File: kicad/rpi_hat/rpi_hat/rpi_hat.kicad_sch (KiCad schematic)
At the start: 12 parts, among them J1 FrontButtons, J2 PowerButton, J3 PowerWakeup, J4 DisplaySPI, J5 BatteryLevel, J6 GPIO, Q1 AO3401A, Q2 PN2222A

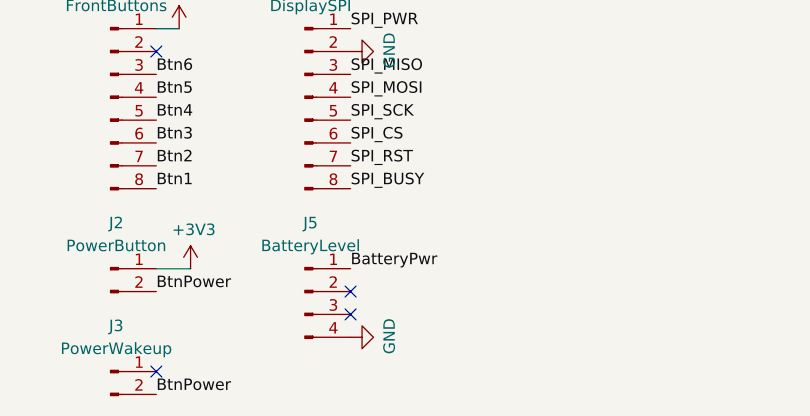
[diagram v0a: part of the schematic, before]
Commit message: add script to read voltage from adc and fix hat
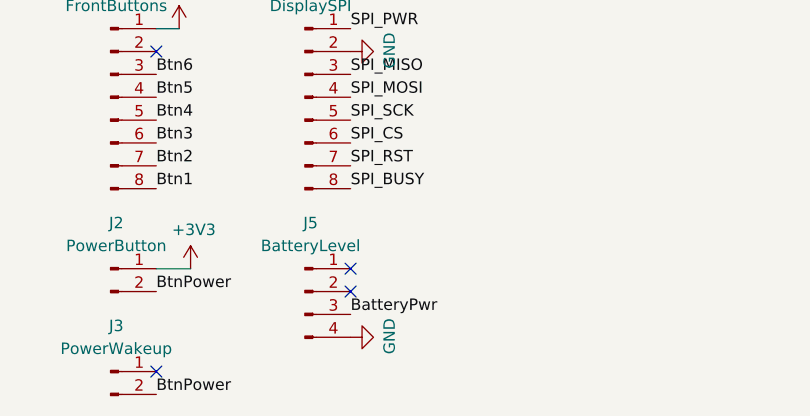
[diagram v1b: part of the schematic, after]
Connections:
- net BatteryPwr: now also J5.3 (Pin_3); no longer J5.1 (Pin_1)
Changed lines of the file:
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@@
+	)
+	(no_connect
+		(at 67.31 134.62)
 	)
 	(no_connect
@@
 	(no_connect
 		(at 109.22 88.9)
-	)
-	(no_connect
-		(at 67.31 139.7)
 	)
 	(no_connect
@@
 		)
 	)
-	(label "BatteryPwr"
-		(at 67.31 134.62 0)
-		(effects
-			(font
-				(size 1.27 1.27)
-			)
-			(justify left bottom)
-		)
-	)
 	(label "GPIO14{slash}TXD0"
 		(at 109.22 50.8 180)
@@
 		(effects
 			(font
+				(size 1.27 1.27)
+			)
+			(justify left bottom)
+		)
+	)
+	(label "BatteryPwr"
+		(at 67.31 139.7 0)
+		(effects
+			(font

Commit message: wip
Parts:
- added R5: 10k, Resistor_THT:R_Axial_DIN0207_L6.3mm_D2.5mm_P10.16mm_Horizontal, symbol Device:R
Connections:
- net +3V3: no longer J2.1 (Pin_1)
- net BtnPower: now also J2.1 (Pin_1), R5.2; no longer J2.2 (Pin_2), J3.2 (Pin_2)
- net GND: now also J2.2 (Pin_2)
- net at J3.1 (Pin_1): now also R5.1

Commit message: finish battery support
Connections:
- net GND: no longer J5.4 (Pin_4), J6.33 (Pin_33), R2.1
- new net BatterNNP16: J5.4 (Pin_4), J6.33 (Pin_33), R2.1
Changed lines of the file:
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@@
+		)
+	)
+	(label "BatteryGND"
+		(at 67.31 142.24 0)
+		(effects
+			(font
+				(size 1.27 1.27)
+			)
+			(justify left bottom)
 		)
 	)
@@
 			)
 			(justify left bottom)
+		)
+	)
+	(label "BatteryGND"
+		(at 187.96 139.7 270)
+		(effects
+			(font
+				(size 1.27 1.27)
+			)
+			(justify right bottom)
 		)
 	)
@@
 	)
 	(symbol
-		(lib_id "power:GND")
-		(at 187.96 139.7 0)
-		(unit 1)
-		(body_style 1)
-		(exclude_from_sim no)
-		(in_bom yes)
-		(on_board yes)
-		(in_pos_files yes)
-		(dnp no)
-		(property "Reference" "#PWR08"
-			(at 187.96 146.05 0)
-			(hide yes)
-			(show_name no)
-			(do_not_autoplace no)
-			(effects
-				(font
-					(size 1.27 1.27)
-				)
-			)
-		)
-		(property "Value" "GND"
-			(at 188.0743 144.0244 0)
-			(show_name no)
-			(do_not_autoplace no)
-			(effects
-				(font
-					(size 1.27 1.27)
-				)
-			)
-		)
-		(property "Footprint" ""
-			(at 187.96 139.7 0)
-			(show_name no)
-			(do_not_autoplace no)
-			(effects
-				(font
-					(size 1.27 1.27)
-				)
-			)
-		)
-		(property "Datasheet" ""
-			(at 187.96 139.7 0)
-			(show_name no)
-			(do_not_autoplace no)
-			(effects
-				(font
-					(size 1.27 1.27)
-				)
-			)
-		)
-		(property "Description" "Power symbol creates a global label with name \"GND\" , ground"
-			(at 187.96 139.7 0)
-			(hide yes)
-			(show_name no)
-			(do_not_autoplace no)
-			(effects
-				(font
-					(size 1.27 1.27)
-				)
-			)
-		)
-		(pin "1"
-		)
-		(instances
-			(project "rpi_hat"
-				(path "/e63e39d7-6ac0-4ffd-8aa3-1841a4541b55"
-					(reference "#PWR08")
-					(unit 1)
-				)
-			)
-		)
-	)
-	(symbol
 		(lib_id "Device:R")
 		(at 187.96 128.27 180)
@@
 					(unit 1)
 				)
-			)
-		)
-	)
-	(symbol
-		(lib_id "power:GND")
-		(at 67.31 142.24 90)
-		(unit 1)
-		(body_style 1)
-		(exclude_from_sim no)
-		(in_bom yes)
-		(on_board yes)
-		(in_pos_files yes)
-		(dnp no)
-		(property "Reference" "#PWR09"
-			(at 73.66 142.24 0)
-			(hide yes)
-			(show_name no)
-			(do_not_autoplace no)
-			(effects
-				(font
-					(size 1.27 1.27)
-				)
-			)
-		)
-		(property "Value" "GND"
-			(at 71.6344 142.1257 0)
-			(show_name no)
-			(do_not_autoplace no)
-			(effects
-				(font
-					(size 1.27 1.27)
-				)
-			)
-		)
-		(property "Footprint" ""
-			(at 67.31 142.24 0)
-			(show_name no)
-			(do_not_autoplace no)
-			(effects
-				(font
-					(size 1.27 1.27)
-				)
-			)
-		)
-		(property "Datasheet" ""
-			(at 67.31 142.24 0)
-			(show_name no)
-			(do_not_autoplace no)
-			(effects
-				(font
-					(size 1.27 1.27)
-				)
-			)
-		)
-		(property "Description" "Power symbol creates a global label with name \"GND\" , ground"
-			(at 67.31 142.24 0)
-			(hide yes)
-			(show_name no)
-			(do_not_autoplace no)
-			(effects
-				(font
-					(size 1.27 1.27)
-				)
-			)
-		)
-		(pin "1"
-		)
-		(instances
-			(project "rpi_hat"
-				(path "/e63e39d7-6ac0-4ffd-8aa3-1841a4541b55"
-					(reference "#PWR09")
-					(unit 1)
-				)
